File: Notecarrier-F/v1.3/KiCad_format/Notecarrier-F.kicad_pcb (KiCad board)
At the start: 4 copper layers, 50.8 x 103 mm, 170 parts, among them J1 S2BPHSM4TBLFSN, J10 CES-124-01-S-S, J11 CES-102-01-S-S, J2 S2BPHSM4TBLFSN, J3 S2BPHSM4TBLFSN, J4 10118193-0001LF, J5 SF72S006VBDR2500, J6 MDT420E01001, J7 SM04B-SRSS-TB(LF)(SN), J8 SM04B-SRSS-TB(LF)(SN), J9 CES-124-01-S-S, SW1 CJS-1200TA, SW2 EVP-BB2A9B000, SW3 CJS-1200TA, SW4 CJS-1200TA, U1 TXS0102DCUR, U2 BQ24210DQCT, U3 TPS63020DSJR, U4 TXS0102DCUR, U5 DGQ2788AEN-T1-GE4, U6 DGQ2788AEN-T1-GE4, U7 MAX17225ELT+, U8 TPS62748YFPT

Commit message: Upgrade the four original ports to KiCad 9; fix F v1.3 DRC; document F errata
Notecarrier-A v2.0, -B v2.1, -F v1.3 and -Pi v1.1 were authored in KiCad 7 and
are now upgraded in place (board 20221018 -> 20241229, schematics -> 20250114).
The upgrade is verified lossless on all four:

- every fabrication layer (copper, mask, paste, silk, Edge.Cuts) is
  geometrically identical before and after at 600 dpi, and drill files are
  textually identical;
- schematic netlists are unchanged - same components, same net partitions
  (A 99/114, B 62/87, F 110/166, Pi 46/95);
- kicanvas renders and the RAG extract both still pass.

Zones are NOT refilled - these ports depend on preserved fills.

Notecarrier-F: the board's 54 net-less 0.6 mm copper patches (footprint
weird-no-fill-via_Fv1.2) sit inside GND copper and are now assigned the GND net
they belong to. DRC goes from 171 errors to 0 with no change to any copper
geometry.

Notecarrier-F ERRATA.md (new): the power section does not match the shipped
board. U9 (AP2139AK-3.3 LDO) with C33/C34, and DS7 (STPS3H100U), are missing
from both schematic and board though they are in the Altium source, the released
BOM, the released pick-and-place, and the shipped copper/mask/paste. All six
diodes carry the wrong part and package: the released design uses FSV1045V in
TO277-3 (3 pads) for DS1/DS2/DS4/DS5 and STPS3H100U in SMB for DS3/DS6/DS7,
where the port has B360A-13-F in DO-214AC SMA (2 pads) throughout. The errata
records the exact wiring and coordinates needed to fix it. Flagged in the root
README and the port's README.

Also documented per port: the DRC exclusions recorded by KiCad 7 no longer
suppress anything, because KiCad 9 computes different marker keys. They are left
as the author's record and the remaining violations are explained in each
Porting-Notes - including evidence that A's J9 pad-vs-zone reports are
preserved-fill artifacts (its In1 plane matches the shipped GND film to within
0.9% of lit area), and that B's 4 error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
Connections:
- REF** pad : (no net) -> GND (x54)

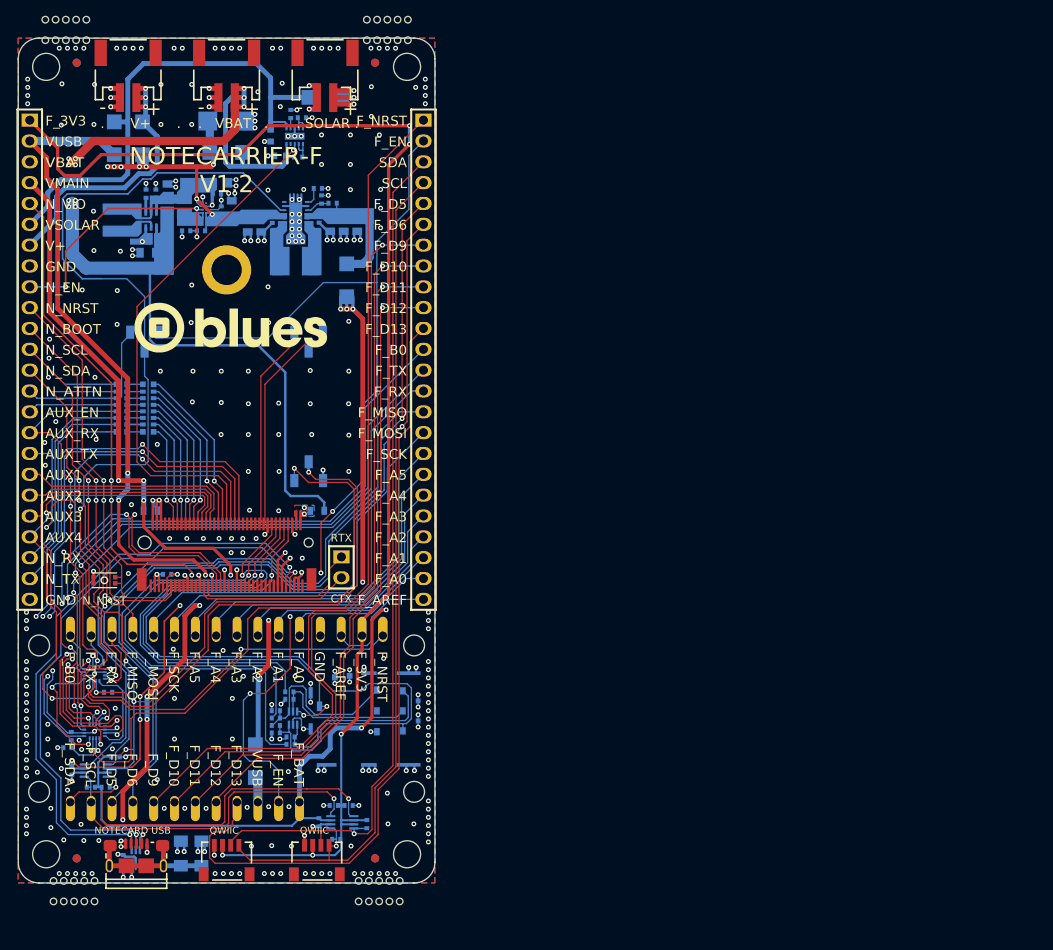
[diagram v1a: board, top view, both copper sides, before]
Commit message: Notecarrier-F v1.3: KiCad 9 port from the release-day Altium sources
Replace the hand-made KiCad 7 port (which described v1.2, with a half-applied
v1.3 schematic delta and an ERRATA file) with a direct import of the v1.3
Altium project, recovered from the design archive's history: committed by the
design house on 2023-07-10, the day of the 2200-814 fabrication package, with a
Rev 11 schematic PDF byte-identical to the one published here. The Altium
sources are published alongside as Notecarrier-F/v1.3/Altium, as for v1.5.

The port follows the v1.5 procedure (KiCad 9.0.9 Altium project importer plus
scripted cleanup, scripts kept under documentation/scripts). All validation
gates pass: ERC 0, DRC 0 with schematic parity, BOM exact (94/94 vs
3000-653-002), placement 89/89 vs PNP-3000-653-002, gerber diff exact on outer
copper and masks with the reviewed inner-annulus/silk classes frozen as the
baseline, KiCanvas and RAG. The KiCad netlist was also matched pad by pad
against the nets carried by the Altium board file (0 conflicts).

J9/J10 are fitted per the released BOM (the 2023-08-31 re-save of the project
flips the variant to match); J11/R11/R12 are DNP. Design rules follow the
board's own Altium rule set (0.1 mm clearance). The old hand-port notes are
kept as History_Porting-Notes-hand-port.md because the harness README cites
them for the gerber-diff recipe; the RAG exclusion comment and the product
README are updated accordingly.

Co-Authored-By: Claude Fable 5.1 <noreply@anthropic.com>
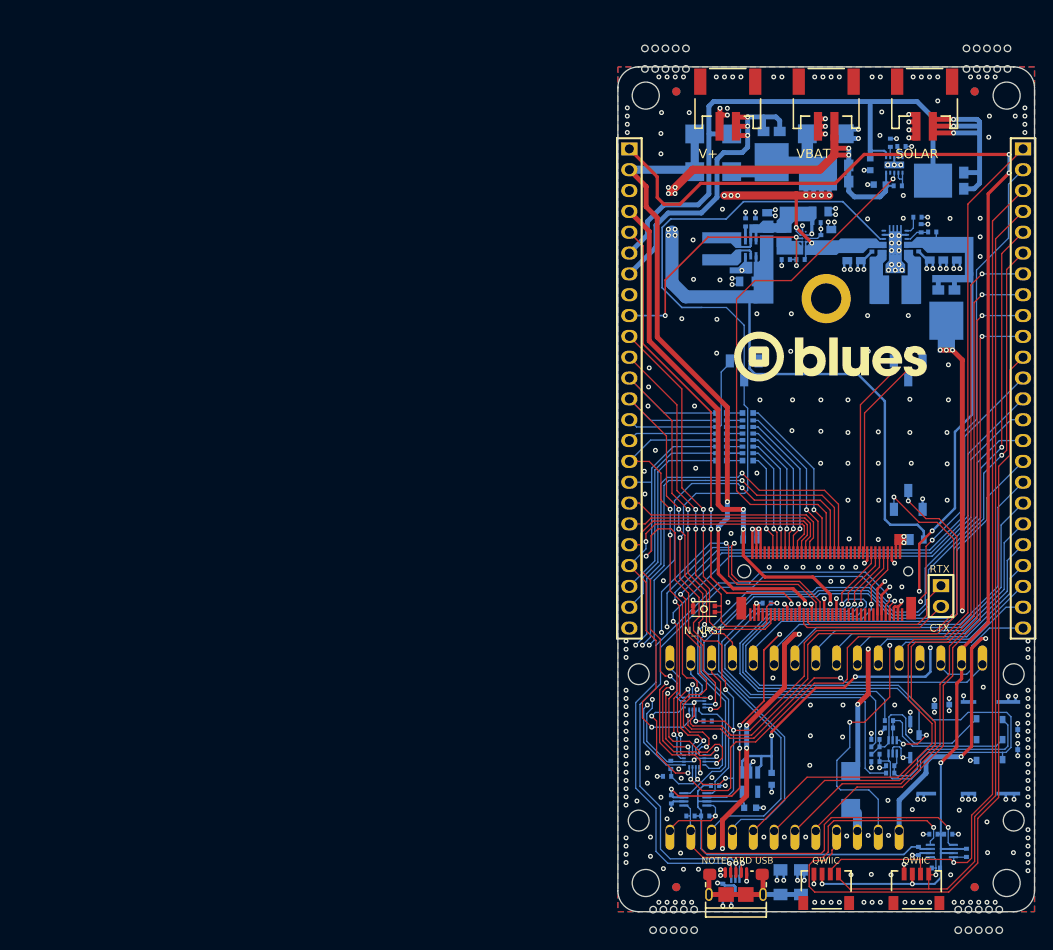
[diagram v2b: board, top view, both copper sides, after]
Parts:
- removed FID1, FID2, FID3, FID4, FID5, FID6, FID7, FID8: TPS, blues-kicad-lib:Fiducial mark 1mm_Fv1.2
- removed G1: Logo, blues-kicad-lib:Logo_23.5x6.1
- removed H5_1, H5_2, H5_3, H5_4: MountingHole, blues-kicad-lib:MountingHole_2.54mm_no-courtyard
- removed REF** (x56): weird-no-fill-via_Fv1.2, blues-kicad-lib:weird-no-fill-via_Fv1.2
- removed REF** (x4): mouse-bite-5x0.8P1.25, blues-kicad-lib:mouse-bite-5x0.8P1.25_Fv1.2
- added C33: 1u, Notecarrier-F-altium-import:C-0603, B.Cu at (141.9, 140.3)
- added C34: 1u, Notecarrier-F-altium-import:C-0603, B.Cu at (139.2, 143.8)
- added DS7: STPS3H100U, Notecarrier-F-altium-import:SMB, B.Cu at (134.7, 66.3)
- added FD1: Fiducial mark, Notecarrier-F-altium-import:Fiducial mark 1mm, F.Cu at (166.6, 56.5)
- added FD2: Fiducial mark, Notecarrier-F-altium-import:Fiducial mark 1mm, F.Cu at (130.2, 56.5)
- added FD3: Fiducial mark, Notecarrier-F-altium-import:Fiducial mark 1mm, F.Cu at (166.6, 153.5)
- added FD4: Fiducial mark, Notecarrier-F-altium-import:Fiducial mark 1mm, F.Cu at (130.2, 153.5)
- added FD5: Fiducial mark, Notecarrier-F-altium-import:Fiducial mark 1mm, B.Cu at (130.2, 56.5)
- added FD6: Fiducial mark, Notecarrier-F-altium-import:Fiducial mark 1mm, B.Cu at (166.6, 56.5)
- added FD7: Fiducial mark, Notecarrier-F-altium-import:Fiducial mark 1mm, B.Cu at (166.6, 153.5)
- added FD8: Fiducial mark, Notecarrier-F-altium-import:Fiducial mark 1mm, B.Cu at (130.2, 153.5)
- added H10: NPTH_free_hole, Notecarrier-F-altium-import:NPTH_free_hole, F.Cu at (170.6, 51.3)
- added H11: NPTH_free_hole, Notecarrier-F-altium-import:NPTH_free_hole, F.Cu at (126.4, 53.8)
- added H12: NPTH_free_hole, Notecarrier-F-altium-import:NPTH_free_hole, F.Cu at (127.7, 53.8)
- added H13: NPTH_free_hole, Notecarrier-F-altium-import:NPTH_free_hole, F.Cu at (128.9, 53.8)
- added H14: NPTH_free_hole, Notecarrier-F-altium-import:NPTH_free_hole, F.Cu at (130.2, 53.8)
- added H15: NPTH_free_hole, Notecarrier-F-altium-import:NPTH_free_hole, F.Cu at (131.4, 53.8)
- added H16: NPTH_free_hole, Notecarrier-F-altium-import:NPTH_free_hole, F.Cu at (165.6, 53.8)
- added H17: NPTH_free_hole, Notecarrier-F-altium-import:NPTH_free_hole, F.Cu at (166.9, 53.8)
- added H18: NPTH_free_hole, Notecarrier-F-altium-import:NPTH_free_hole, F.Cu at (168.1, 53.8)
- added H19: NPTH_free_hole, Notecarrier-F-altium-import:NPTH_free_hole, F.Cu at (169.4, 53.8)
- added H20: NPTH_free_hole, Notecarrier-F-altium-import:NPTH_free_hole, F.Cu at (170.6, 53.8)
- added H21: NPTH_free_hole_3.3mm, Notecarrier-F-altium-import:NPTH_free_hole_3.3mm, F.Cu at (126.5, 57.0)
- added H22: NPTH_free_hole_3.3mm, Notecarrier-F-altium-import:NPTH_free_hole_3.3mm, F.Cu at (170.5, 57.0)
- added H23: NPTH_free_hole_2.54mm, Notecarrier-F-altium-import:NPTH_free_hole_2.54mm, F.Cu at (125.6, 127.5)
- added H24: NPTH_free_hole_2.54mm, Notecarrier-F-altium-import:NPTH_free_hole_2.54mm, F.Cu at (171.4, 127.5)
- added H25: NPTH_free_hole_2.54mm, Notecarrier-F-altium-import:NPTH_free_hole_2.54mm, F.Cu at (125.6, 145.4)
- added H26: NPTH_free_hole_2.54mm, Notecarrier-F-altium-import:NPTH_free_hole_2.54mm, F.Cu at (171.4, 145.4)
- added H27: NPTH_free_hole_3.3mm, Notecarrier-F-altium-import:NPTH_free_hole_3.3mm, F.Cu at (126.5, 153.0)
- added H28: NPTH_free_hole_3.3mm, Notecarrier-F-altium-import:NPTH_free_hole_3.3mm, F.Cu at (170.5, 153.0)
- added H29: NPTH_free_hole, Notecarrier-F-altium-import:NPTH_free_hole, F.Cu at (127.4, 156.3)
- added H30: NPTH_free_hole, Notecarrier-F-altium-import:NPTH_free_hole, F.Cu at (128.7, 156.3)
- added H31: NPTH_free_hole, Notecarrier-F-altium-import:NPTH_free_hole, F.Cu at (129.9, 156.3)
- added H32: NPTH_free_hole, Notecarrier-F-altium-import:NPTH_free_hole, F.Cu at (131.2, 156.3)
- added H33: NPTH_free_hole, Notecarrier-F-altium-import:NPTH_free_hole, F.Cu at (132.4, 156.3)
- added H34: NPTH_free_hole, Notecarrier-F-altium-import:NPTH_free_hole, F.Cu at (164.6, 156.3)
- added H35: NPTH_free_hole, Notecarrier-F-altium-import:NPTH_free_hole, F.Cu at (165.9, 156.3)
- added H36: NPTH_free_hole, Notecarrier-F-altium-import:NPTH_free_hole, F.Cu at (167.1, 156.3)
- added H37: NPTH_free_hole, Notecarrier-F-altium-import:NPTH_free_hole, F.Cu at (168.4, 156.3)
- added H38: NPTH_free_hole, Notecarrier-F-altium-import:NPTH_free_hole, F.Cu at (169.6, 156.3)
- added H39: NPTH_free_hole, Notecarrier-F-altium-import:NPTH_free_hole, F.Cu at (127.4, 158.8)
- added H40: NPTH_free_hole, Notecarrier-F-altium-import:NPTH_free_hole, F.Cu at (128.7, 158.8)
- added H41: NPTH_free_hole, Notecarrier-F-altium-import:NPTH_free_hole, F.Cu at (129.9, 158.8)
- added H42: NPTH_free_hole, Notecarrier-F-altium-import:NPTH_free_hole, F.Cu at (131.2, 158.8)
- added H43: NPTH_free_hole, Notecarrier-F-altium-import:NPTH_free_hole, F.Cu at (132.4, 158.8)
- added H44: NPTH_free_hole, Notecarrier-F-altium-import:NPTH_free_hole, F.Cu at (164.6, 158.8)
- added H45: NPTH_free_hole, Notecarrier-F-altium-import:NPTH_free_hole, F.Cu at (165.9, 158.8)
- added H46: NPTH_free_hole, Notecarrier-F-altium-import:NPTH_free_hole, F.Cu at (167.1, 158.8)
- added H47: NPTH_free_hole, Notecarrier-F-altium-import:NPTH_free_hole, F.Cu at (168.4, 158.8)
- added H48: NPTH_free_hole, Notecarrier-F-altium-import:NPTH_free_hole, F.Cu at (169.6, 158.8)
- added H5: NPTH_free_hole, Notecarrier-F-altium-import:NPTH_free_hole, F.Cu at (131.4, 51.3)
- added H6: NPTH_free_hole, Notecarrier-F-altium-import:NPTH_free_hole, F.Cu at (165.6, 51.3)
- added H7: NPTH_free_hole, Notecarrier-F-altium-import:NPTH_free_hole, F.Cu at (166.9, 51.3)
- added H8: NPTH_free_hole, Notecarrier-F-altium-import:NPTH_free_hole, F.Cu at (168.1, 51.3)
- added H9: NPTH_free_hole, Notecarrier-F-altium-import:NPTH_free_hole, F.Cu at (169.4, 51.3)
- added U9: AP2139AK-3.3TRG1, Notecarrier-F-altium-import:SOT-23-5(M5), B.Cu at (139.2, 140.7)
- C1, C2: value 1µF -> 1u; footprint blues-kicad-lib:C-0603_Fv1.2 -> Notecarrier-F-altium-import:C-0603
- C10, C11, C12, C13, C14, C15, C18, C19, C25, C26, C28, C3, C30, C31, C32, C5, C9: value 0.1µF -> 100n; footprint blues-kicad-lib:C-0402_Fv1.2 -> Notecarrier-F-altium-import:C-0402
- C16, C17, C20, C21, C22, C23, C24, C27, C29: value 22µF -> 22u; footprint blues-kicad-lib:C-0805_Fv1.2 -> Notecarrier-F-altium-import:C-0805
- C4: value 10nF/1000V -> 10n/1000V; footprint blues-kicad-lib:C-1206_Fv1.2 -> Notecarrier-F-altium-import:C-1206
- C6, C7, C8: value 33pF -> 33p; footprint blues-kicad-lib:C-0402_Fv1.2 -> Notecarrier-F-altium-import:C-0402
- DS1, DS2, DS4, DS5: value B360A-13-F -> FSV1045V; footprint blues-kicad-lib:DO-214AC SMA_Fv1.2 -> Notecarrier-F-altium-import:TO277-3
- DS3, DS6: value B360A-13-F -> STPS3H100U; footprint blues-kicad-lib:DO-214AC SMA_Fv1.2 -> Notecarrier-F-altium-import:SMB
- F1: value F1.5A -> SF-0603F150-2; footprint blues-kicad-lib:FS-0603_Fv1.2 -> Notecarrier-F-altium-import:FS-0603
- F2: footprint blues-kicad-lib:FS-0603_Fv1.2 -> Notecarrier-F-altium-import:FS-0603
- H1, H2, H3, H4: value MountingHole -> NPTH_free_hole; footprint blues-kicad-lib:MountingHole_3.3mm_no-courtyard -> Notecarrier-F-altium-import:NPTH_free_hole
- J1, J2, J3: footprint blues-kicad-lib:JST S2B-PH-SM4-TB_Fv1.2 -> Notecarrier-F-altium-import:JST S2B-PH-SM4-TB
- J10, J9: footprint blues-kicad-lib:CES-124-01-S-S_Fv1.2 -> Notecarrier-F-altium-import:CES-124-01-S-S
- J11: footprint blues-kicad-lib:CONN_02_Fv1.2 -> Notecarrier-F-altium-import:CONN_02
- J4: footprint blues-kicad-lib:FCI USB 10118193-0001LF_Fv1.2 -> Notecarrier-F-altium-import:FCI USB 10118193-0001LF
- J5: footprint blues-kicad-lib:J-NANOSIM-SF72S006VBA_Fv1.2 -> Notecarrier-F-altium-import:J-NANOSIM-SF72S006VBA
- J6: footprint blues-kicad-lib:J-75-0050-MOS-M2_Fv1.2 -> Notecarrier-F-altium-import:J-75-0050-MOS-M2
- J7, J8: footprint blues-kicad-lib:JST SM04B-SRSS-TB_Fv1.2 -> Notecarrier-F-altium-import:JST SM04B-SRSS-TB
- L1: value 2.2µH -> 2u2; footprint blues-kicad-lib:IND_XFL4020-222MEC_Fv1.2 -> Notecarrier-F-altium-import:IND_XFL4020-222MEC
- L2: footprint blues-kicad-lib:VCHA042A-1R5MS6_Fv1.2 -> Notecarrier-F-altium-import:VCHA042A-1R5MS6
- L3: value 2.2µH -> 2u2; footprint blues-kicad-lib:1285AS-H-2R2M=P2-INDC2016X100N_Fv1.2 -> Notecarrier-F-altium-import:1285AS-H-2R2M=P2-INDC2016X100N
- MOD2: footprint blues-kicad-lib:BLUES_WIRELESS_SWAN_2-54_HEADERS_Fv1.2 -> Notecarrier-F-altium-import:BLUES_WIRELESS_SWAN_2-54_HEADERS
- MODL1: footprint blues-kicad-lib:16PIN_254MM_Fv1.2 -> Notecarrier-F-altium-import:16PIN_254MM
- MODR1: footprint blues-kicad-lib:12PIN_254MM_Fv1.2 -> Notecarrier-F-altium-import:12PIN_254MM
- OBJ1: footprint blues-kicad-lib:DIST-WASMSIM0250_Fv1.2 -> Notecarrier-F-altium-import:DIST-WASMSIM0250
- R1, R20: footprint blues-kicad-lib:RESCAXS80P640X160X50-16N_Fv1.2 -> Notecarrier-F-altium-import:RESCAXS80P640X160X50-16N
- R10, R11, R12, R14, R15, R16, R17, R18, R19, R2, R4, R6, R7, R8, R9: footprint blues-kicad-lib:R-0402_Fv1.2 -> Notecarrier-F-altium-import:R-0402
- R13: value 1.1M -> 1M1; footprint blues-kicad-lib:R-0402_Fv1.2 -> Notecarrier-F-altium-import:R-0402
- R3: value 499R -> 470R; footprint blues-kicad-lib:R-0402_Fv1.2 -> Notecarrier-F-altium-import:R-0402
- R5: footprint blues-kicad-lib:R-1206_Fv1.2 -> Notecarrier-F-altium-import:R-1206
- SW1, SW3, SW4: footprint blues-kicad-lib:SW_CJS-1200TA_Fv1.2 -> Notecarrier-F-altium-import:SW_CJS-1200TA
- SW2: footprint blues-kicad-lib:SW_EVP-BB2A9B000_Fv1.2 -> Notecarrier-F-altium-import:SW_EVP-BB2A9B000
- TVS1: footprint blues-kicad-lib:SMB_Fv1.2 -> Notecarrier-F-altium-import:SMB
- TVS2, TVS3: footprint blues-kicad-lib:SOT666_Fv1.2 -> Notecarrier-F-altium-import:SOT666
- U1, U4: footprint blues-kicad-lib:SOP50P310X90-8N_Fv1.2 -> Notecarrier-F-altium-import:SOP50P310X90-8N
- U2: footprint blues-kicad-lib:WSON10-EXP_Fv1.2 -> Notecarrier-F-altium-import:WSON10-EXP
- U3: footprint blues-kicad-lib:TI PVSON-14 DSJ_Fv1.2 -> Notecarrier-F-altium-import:TI PVSON-14 DSJ
- U5, U6: footprint blues-kicad-lib:QFN40P260X180X60-16N_Fv1.2 -> Notecarrier-F-altium-import:QFN40P260X180X60-16N
- U7: footprint blues-kicad-lib:MAX17225ELT+UDFN_Fv1.2 -> Notecarrier-F-altium-import:MAX17225ELT+UDFN
- U8: footprint blues-kicad-lib:TPS62748YFPT-DSBGA4x2_Fv1.2 -> Notecarrier-F-altium-import:TPS62748YFPT-DSBGA4x2
- moved H4 124.7 mm to (130.2, 51.3)
- moved H3 103.2 mm to (128.9, 51.3)
- moved DS1 76.7 mm to (141.9, 64.1), turned to 0 degrees
- moved DS4 75.8 mm to (162.5, 67.4), turned to -90 degrees
- moved DS5 73.2 mm to (163.2, 83.5), turned to 0 degrees
- moved DS2 73.2 mm to (148.5, 66.5), turned to -90 degrees
- moved C27 73.2 mm to (149.1, 74.3)
- moved C28 73.2 mm to (139.9, 72.5)
- moved F2 73.2 mm to (139.2, 111.1)
- moved R19 73.2 mm to (145.4, 77.0)
- moved C19 73.2 mm to (139.5, 78.4)
- moved C29 73.2 mm to (138.9, 79.7), turned to 180 degrees
- moved U6 73.2 mm to (132.4, 131.0)
- moved SW2 73.2 mm to (133.6, 119.6)
- moved SW1 73.2 mm to (158.5, 90.5)
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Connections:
- net /Feather/ALT_DFU_ACTIVE renamed ALT_DFU_ACTIVE
- net /Feather/ALT_DFU_BOOT renamed ALT_DFU_BOOT
- net /Feather/ALT_DFU_RESET renamed ALT_DFU_RESET
- net /Feather/ALT_DFU_RX renamed ALT_DFU_RX
- net /Feather/ALT_DFU_TX renamed ALT_DFU_TX
- net /Feather/DFU_SW renamed /Feather Connection/DFU_SW
- net /Feather/EN_F_BAT renamed EN_F_BAT
- net /Feather/F_A0 renamed F_A0
- net /Feather/F_A1 renamed F_A1
- net /Feather/F_A2 renamed F_A2
- net /Feather/F_A3 renamed F_A3
- net /Feather/F_A4 renamed F_A4
- net /Feather/F_A5 renamed F_A5
- net /Feather/F_AREF renamed F_AREF
- net /Feather/F_B0 renamed /Feather Connection/F_B0
- net /Feather/F_B0_SW renamed F_B0_SW
- net /Feather/F_D10 renamed F_D10
- net /Feather/F_D11 renamed F_D11
- net /Feather/F_D12 renamed F_D12
- net /Feather/F_D13 renamed F_D13
- net /Feather/F_D5 renamed F_D5
- net /Feather/F_D6 renamed F_D6
- net /Feather/F_D9 renamed F_D9
- net /Feather/F_MISO renamed F_MISO
- net /Feather/F_MOSI renamed F_MOSI
- net /Feather/F_NRST renamed F_NRST
- net /Feather/F_NRST_SW renamed F_NRST_SW
- net /Feather/F_RX renamed /Feather Connection/F_RX
- net /Feather/F_RX_SW renamed F_RX_SW
- net /Feather/F_SCK renamed F_SCK
- net /Feather/F_SCL renamed /Feather Connection/F_SCL
- net /Feather/F_SDA renamed /Feather Connection/F_SDA
- net /Feather/F_TX renamed /Feather Connection/F_TX
- net /Feather/F_TX_SW renamed F_TX_SW
- net /Feather/N_ATTN renamed N_ATTN
- net /Feather/N_AUX3 renamed N_AUX3
- net /Feather/N_AUX4 renamed N_AUX4
- net /Feather/N_AUX_RX renamed N_AUX_RX
- net /Feather/N_AUX_TX renamed N_AUX_TX
- net /Feather/SW_SDA renamed SW_SDA
- net /IO/N_AUX_EN renamed N_AUX_EN
- net /IO/N_BOOT renamed N_BOOT
- net /IO/N_NRST renamed N_NRST
- net /IO/N_RX renamed N_RX
- net /IO/N_TX renamed N_TX
- net /Notecard/ATTN_P renamed /Notecard Connection/ATTN_P
- net /Notecard/AUX_CHARGING renamed AUX_CHARGING
- net /Notecard/AUX_EN_P renamed /Notecard Connection/AUX_EN_P
- net /Notecard/AUX_RX_P renamed /Notecard Connection/AUX_RX_P
- net /Notecard/AUX_TX_P renamed /Notecard Connection/AUX_TX_P
- net /Notecard/CTX renamed /Notecard Connection/CTX
- net /Notecard/D_N renamed D_N
- net /Notecard/D_P renamed D_P
- net /Notecard/N_AUX1 renamed N_AUX1
- net /Notecard/N_AUX2 renamed N_AUX2
- net /Notecard/N_SCL renamed N_SCL
- net /Notecard/N_SDA renamed N_SDA
- net /Notecard/RTX renamed /Notecard Connection/RTX
- net /Notecard/RX_P renamed /Notecard Connection/RX_P
- net /Notecard/SIM_CLK renamed /Notecard Connection/SIM_CLK
- net /Notecard/SIM_IO renamed /Notecard Connection/SIM_IO
- net /Notecard/SIM_RST renamed /Notecard Connection/SIM_RST
- net /Notecard/TX_P renamed /Notecard Connection/TX_P
- C11 pad 1: F_BAT -> F_VIO
- C14 pad 1: F_BAT -> F_VIO
- C22 pad 1: Net-(DS5-A) -> Net-(DS5-A1)
- C23 pad 1: Net-(DS5-A) -> Net-(DS5-A1)
- C24 pad 1: Net-(DS5-A) -> Net-(DS5-A1)
- C25 pad 2: Net-(DS5-A) -> Net-(DS5-A1)
- C26 pad 1: VMAIN -> GND
- C26 pad 2: GND -> VMAIN
- C29 pad 1: GND -> N_VIO
- C29 pad 2: N_VIO -> GND
- C31 pad 1: /N_EN -> GND
- C31 pad 2: GND -> N_EN
- C5 pad 2: /Notecard/SIM_VCC -> /Notecard Connection/SIM_VCC
- C8 pad 2: Net-(J5-I/O) -> Net-(J5-IO)
- DS1 pad 2: VMAIN -> V+
- DS2 pad 2: VMAIN -> VBAT
- DS3 pad 1: VUSB -> VSOLAR
- DS3 pad 2: VSOLAR -> VUSB
- DS4 pad 1: Net-(DS4-A) -> Net-(DS4-A1)
- DS4 pad 2: VSOLAR -> Net-(DS4-A1)
- DS5 pad 1: Net-(DS5-A) -> Net-(DS5-A1)
- DS5 pad 2: F_BAT -> Net-(DS5-A1)
- DS6 pad 1: /Feather/F_VUSB -> VMAIN
- DS6 pad 2: VMAIN -> F_VUSB
- J10 pad 9: /N_EN -> N_EN
- J2 pad 2: Net-(DS4-A) -> Net-(DS4-A1)
- J6 pad 1: unconnected-(J6-NC1-Pad1) -> (no net)
- J6 pad 15: unconnected-(J6-NC15-Pad15) -> (no net)
- J6 pad 16: /Notecard/SIM_NPRESENT -> /Notecard Connection/SIM_NPRESENT
- J6 pad 17: unconnected-(J6-NC17-Pad17) -> (no net)
- J6 pad 19: unconnected-(J6-NC19-Pad19) -> (no net)
- J6 pad 21: unconnected-(J6-NC21-Pad21) -> (no net)
- J6 pad 23: unconnected-(J6-NC23-Pad23) -> (no net)
- J6 pad 35: unconnected-(J6-NC35-Pad35) -> (no net)
- J6 pad 37: unconnected-(J6-NC37-Pad37) -> (no net)
- J6 pad 44: unconnected-(J6-NC44-Pad44) -> (no net)
- J6 pad 53: unconnected-(J6-NC53-Pad53) -> (no net)
- J6 pad 55: unconnected-(J6-NC55-Pad55) -> (no net)
- J6 pad 59: unconnected-(J6-NC59-Pad59) -> (no net)
- J6 pad 61: unconnected-(J6-NC61-Pad61) -> (no net)
- J6 pad 63: unconnected-(J6-NC63-Pad63) -> (no net)
- J6 pad 66: unconnected-(J6-NC66-Pad66) -> (no net)
- J6 pad 68: unconnected-(J6-NC68-Pad68) -> (no net)
- J6 pad 69: unconnected-(J6-NC69-Pad69) -> (no net)
- J6 pad 75: unconnected-(J6-NC75-Pad75) -> (no net)
- J6 pad 8: /Notecard/SIM_VCC -> /Notecard Connection/SIM_VCC
- J7 pad 1: /Feather/SW_SCL -> SW_SCL
- J8 pad 1: /Feather/SW_SCL -> SW_SCL
- J9 pad 2: /Feather/F_EN -> F_EN
- J9 pad 4: /Feather/SW_SCL -> SW_SCL
- MODR1 pad 2: /Feather/F_EN -> F_EN
- MODR1 pad 3: /Feather/F_VUSB -> F_VUSB
- R11 pad 2: F_BAT -> F_VIO
- R12 pad 2: F_BAT -> F_VIO
- R13 pad 2: Net-(DS5-A) -> Net-(DS5-A1)
- R15 pad 1: F_3V3 -> SW_SCL
- R15 pad 2: /Feather/SW_SCL -> F_3V3
- R19 pad 1: /N_EN -> N_EN
- R6 pad 1: Net-(J5-I/O) -> Net-(J5-IO)
- R6 pad 2: /Notecard/SIM_VCC -> /Notecard Connection/SIM_VCC
- R9 pad 2: Net-(J5-I/O) -> Net-(J5-IO)
- SW1 pad 3: unconnected-(SW1-A-Pad3) -> (no net)
- SW3 pad 3: /Feather/F_EN -> N_VIO
- TVS2 pad 3: /Notecard/SIM_VCC -> /Notecard Connection/SIM_VCC
- TVS2 pad 4: Net-(J5-I/O) -> Net-(J5-IO)
- TVS2 pad 6: /Notecard/SIM_NPRESENT -> /Notecard Connection/SIM_NPRESENT
- TVS3 pad 1: unconnected-(TVS3-K1-Pad1) -> (no net)
- U1 pad 1: /Feather/SW_SCL -> SW_SCL
- U1 pad 3: F_BAT -> F_VIO
- U2 pad 9: unconnected-(U2-VDPM-Pad9) -> (no net)
- U3 pad 14: unconnected-(U3-PG-Pad14) -> (no net)
- U3 pad 4: Net-(DS5-A) -> Net-(DS5-A1)
- U3 pad 5: Net-(DS5-A) -> Net-(DS5-A1)
- U4 pad 7: F_BAT -> F_VIO
- U8 pad B1: /N_EN -> N_EN
- U8 pad D2: unconnected-(U8-LOAD-PadD2) -> (no net)
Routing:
- net /Feather/F_EN: track 123.1 -> 0.00 mm, vias 4 -> 0
- net SW_SCL: track 0.00 -> 107.0 mm, vias 0 -> 1
- net /Feather/SW_SCL: track 106.6 -> 0.00 mm, vias 1 -> 0
- net F_EN: track 0.00 -> 95.2 mm, vias 0 -> 4
- net Net-(DS5-A1): track 0.00 -> 90.3 mm, vias 0 -> 5
- net /Notecard/SIM_VCC: track 90.1 -> 0.00 mm, vias 1 -> 0
- net /Notecard Connection/SIM_VCC: track 0.00 -> 90.0 mm, vias 0 -> 1
- net /Notecard Connection/SIM_NPRESENT: track 0.00 -> 63.8 mm, vias 0 -> 3
- net /Notecard/SIM_NPRESENT: track 63.8 -> 0.00 mm, vias 3 -> 0
- net F_VIO: track 0.00 -> 46.1 mm
- net F_BAT: track 114.9 -> 73.1 mm
- net N_EN: track 0.00 -> 32.6 mm, vias 0 -> 3
- net /N_EN: track 32.6 -> 0.00 mm, vias 3 -> 0
- net Net-(DS4-A1): track 0.00 -> 28.6 mm, vias 0 -> 3
- net Net-(J5-I/O): track 21.3 -> 0.00 mm
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- removed copper zone on B.Cu, net Net-(F2-Pad2)
- removed copper zone on B.Cu, net VIO_P
- removed copper zone on F.Cu, net VIO_P
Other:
- board text added: "${PCBA_BOM_NUM}"
- board text added: "${PCB_ACCEPTOR}"
- board text added: "${PCB_AUTHOR}"
- board text added: "${PCB_NUM}"
- board text added: "'.HW_E_Doc_Num' '.Module_Name' Rev. '.HW_E_Doc_Rev'"
- board text added: "0.15 mm"
- board text added: "0.3 mm"
- board text added: "0.300mm (11.81mil)"
- board text added: "0.500mm (19.69mil)"
- board text added: "0.800mm (31.50mil)"
- board text added: "1"
- board text added: "1."
- board text added: "1.000mm (39.37mil)"
- board text added: "1.100mm (43.31mil)"
- board text added: "1.6 (±0.1) mm"
- board text added: "1.600mm (62.99mil)"
- board text added: "10."
- board text added: "10000 Zagreb"
- board text added: "103x50.8 (±0.2) mm"
- board text added: "11."
- board text added: "12."
- board text added: "13."
- board text added: "14."
- board text added: "15"
- board text added: "15."
- board text added: "16."
- board text added: "17."
- board text added: "18."
- board text added: "19."
- board text added: "2"
- board text added: "2."
- board text added: "2.540mm (100.00mil)"
- board text added: "20."
- board text added: "28"
- board text added: "3"
- board text added: "3."
- board text added: "3.300mm (129.92mil)"
- board text added: "3.700mm (145.67mil)"
- board text added: "4."
- board text added: "40"
- board text added: "5."
- board text added: "50"
- board text added: "506"
- board text added: "6."
- board text added: "637 Total"
- board text added: "7."
- board text added: "8."
- board text added: "9."
- board text added: "= Calculated from tool start centre position to tool end centre position."
- board text added: "= Routed Path Length + Tool Size = Slot length as defined in the PCB layout"
- board text added: "A"
- board text added: "A4"
- board text added: "ACCEPTOR:"
- board text added: "AUTHOR:"
- board text added: "Additional requests"
- board text added: "Assembly drawing comments - BOTTOM"
- board text added: "Assembly drawing comments - TOP"
- board text added: "Assembly drawing designators - BOTTOM"
- board text added: "Assembly drawing designators - TOP"
- board text added: "B"
- board text added: "BOM NO.:"
- board text added: "Blind vias"
- board text added: "Board Layer"
- board text added: "Board dimension"
- board text added: "Board thickness"
- board text added: "Bottom Layer"
- board text added: "Bottom Layer (GBL)"
- board text added: "Bottom Overlay (Silk)"
- board text added: "Bottom PSM"
- board text added: "Byte Lab Grupa d.o.o."
- board text added: "C"
- board text added: "Copper"
- board text added: "Core"
- board text added: "Count"
- board text added: "Croatia"
- board text added: "D"
- board text added: "DRR"
- board text added: "Description"
- board text added: "Dielectric"
- board text added: "FORMAT:"
- board text added: "FR-4"
- board text added: "FR-4 (Tg 140)"
- board text added: "File"
- board text added: "G1"
- board text added: "G2"
- board text added: "GBL"
- board text added: "GBO"
- board text added: "GBP"
- board text added: "GBS"
- board text added: "GM10"
- board text added: "GM11"
- board text added: "GM15"
- board text added: "GM16"
- board text added: "GM8"
- board text added: "GM9"
- board text added: "GTL"
- board text added: "GTO"
- board text added: "GTP"
- board text added: "GTS"
- board text added: "Generated"
- board text added: "Gerber specification"
- board text added: "Gerbers Specification"
- board text added: "HAL (lead-free)"
- board text added: "HAL (with lead)"
- board text added: "Half holes/castellated edges"
- board text added: "Hole Length"
- board text added: "Hole Size"
- board text added: "Hole Type"
- board text added: "Impedance control"
- board text added: "Layer name"
- board text added: "Layer stack up details"
- board text added: "List of Gerber files"
- board text added: "Medarska 69/1"
- board text added: "Mid Layer 1"
- board text added: "Mid Layer 1 (G1)"
- board text added: "Mid Layer 2"
- board text added: "Mid Layer 2 (G2)"
- board text added: "Milling"
- board text added: "Min. hole size"
- board text added: "Min. track/spacing"
- board text added: "NCDrill file report"
- board text added: "NPTH"
- board text added: "No."
- board text added: "Number of Gerber Files"
- board text added: "Number of layers"
- board text added: "Other:"
- board text added: "PART NO.:"
- board text added: "PCB requirements"
- board text added: "PTH"
- board text added: "Panelization"
- board text added: "Parameter"
- board text added: "Plated"
- board text added: "Plated edge"
- board text added: "Prepreg"
- board text added: "RoHS compatibility"
- board text added: "Round"
- board text added: "Round holes"
- board text added: "Routed Path Length"
- board text added: "SIGNATURE"
- board text added: "Sheet Top"
- board text added: "Silkscreen bottom"
- board text added: "Silkscreen top"
- board text added: "Slot"
- board text added: "Slot definitions :"
- board text added: "Slot holes"
- board text added: "Solder mask"
- board text added: "Surface finishing"
- board text added: "Symbol"
- board text added: "TITLE:"
- board text added: "TX1"
- board text added: "TXT"
- board text added: "This document is the exclusive property of Byte Lab Grupa d.o.o. Company and it should not be distributed or"
- board text added: "Top Layer"
- board text added: "Top Layer (GTL)"
- board text added: "Top Overlay (Silk)"
- board text added: "V-Cut"
- board text added: "Value"
- board text added: "Via in pad"
- board text added: "Yes"
- board text added: "extension"
- board text added: "height"
- board text added: "material"
- board text added: "other:"
- board text added: "reproduced into any other format without prior permission from Byte Lab Grupa d.o.o."
- board text added: "thickness"
- board text added: "type"
- board text removed: "+"
- board text removed: "-"
- board text removed: ". SOLAR ."
- board text removed: ". V+ ."
- board text removed: ". VBAT ."
- board text removed: "0 mm"
- board text removed: "0.015 mm"
- board text removed: "0.1500 mm"
- board text removed: "0.3000 mm"
- board text removed: "1.6000 mm"
- board text removed: "50.8000 mm x 103.0000 mm"
- board text removed: "AUX1"
- board text removed: "AUX2"
- board text removed: "AUX3"
- board text removed: "AUX4"
- board text removed: "AUX_EN"
- board text removed: "AUX_RX"
- board text removed: "AUX_TX"
- board text removed: "B.Cu"
- board text removed: "B.Mask"
- board text removed: "B.Paste"
- board text removed: "B.Silkscreen"
- board text removed: "BOARD CHARACTERISTICS"
- board text removed: "Board Thickness:"
- board text removed: "Board overall dimensions:"
- board text removed: "Bottom Silk Screen"
- board text removed: "Castellated pads:"
- board text removed: "Color"
- board text removed: "Copper Finish:"
- board text removed: "Copper Layer Count:"
- board text removed: "Dielectric 1"
- board text removed: "Dielectric 2"
- board text removed: "Dielectric 3"
- board text removed: "Edge card connectors:"
- board text removed: "F.Cu"
- board text removed: "F.Mask"
- board text removed: "F.Paste"
- board text removed: "F.Silkscreen"
- board text removed: "FR4 natural"
- board text removed: "FR4-TG140"
- board text removed: "F_3V3"
- board text removed: "F_A0"
- board text removed: "F_A1"
- board text removed: "F_A2"
- board text removed: "F_A3"
- board text removed: "F_A4"
- board text removed: "F_A5"
- board text removed: "F_AREF"
- board text removed: "F_B0"
- board text removed: "F_BAT"
- board text removed: "F_D10"
- board text removed: "F_D11"
- board text removed: "F_D12"
- board text removed: "F_D13"
- board text removed: "F_D5"
- board text removed: "F_D6"
- board text removed: "F_D9"
- board text removed: "F_EN"
- board text removed: "F_MISO"
- board text removed: "F_MOSI"
- board text removed: "F_NRST"
- board text removed: "F_RX"
- board text removed: "F_SCK"
- board text removed: "F_SCL"
- board text removed: "F_SDA"
- board text removed: "F_TX"
- board text removed: "GND"
- board text removed: "Impedance Control:"
- board text removed: "In1.Cu"
- board text removed: "In2.Cu"
- board text removed: "Layer Name"
- board text removed: "Min hole diameter:"
- board text removed: "Min track/spacing:"
- board text removed: "NOTECARRIER-F"
- board text removed: "N_BOOT"
- board text removed: "N_EN"
- board text removed: "N_RX"
- board text removed: "N_SCL"
- board text removed: "N_SDA"
- board text removed: "N_TX"
- board text removed: "N_VIO"
- board text removed: "Not specified"
- board text removed: "Plated Board Edge:"
- board text removed: "SCL"
- board text removed: "SDA"
- board text removed: "Thickness (mm)"
- board text removed: "Top Silk Screen"
- board text removed: "Type"
- board text removed: "V1.2"
- board text removed: "VMAIN"
- board text removed: "VSOLAR"
- board text removed: "VUSB"
- board text removed: "copper"
- board text removed: "core"
- board text removed: "prepreg"
